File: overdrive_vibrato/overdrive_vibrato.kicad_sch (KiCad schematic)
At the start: 27 parts, among them J1 Conn_01x08, Q1 BC547, Q2 BC547, Q3 BC547, SW1 E-SWITCH-SW_Push_LED, SW2 E-SWITCH-SW_Push_LED, SW3 E-SWITCH-SW_Push_LED, U1 74HC14

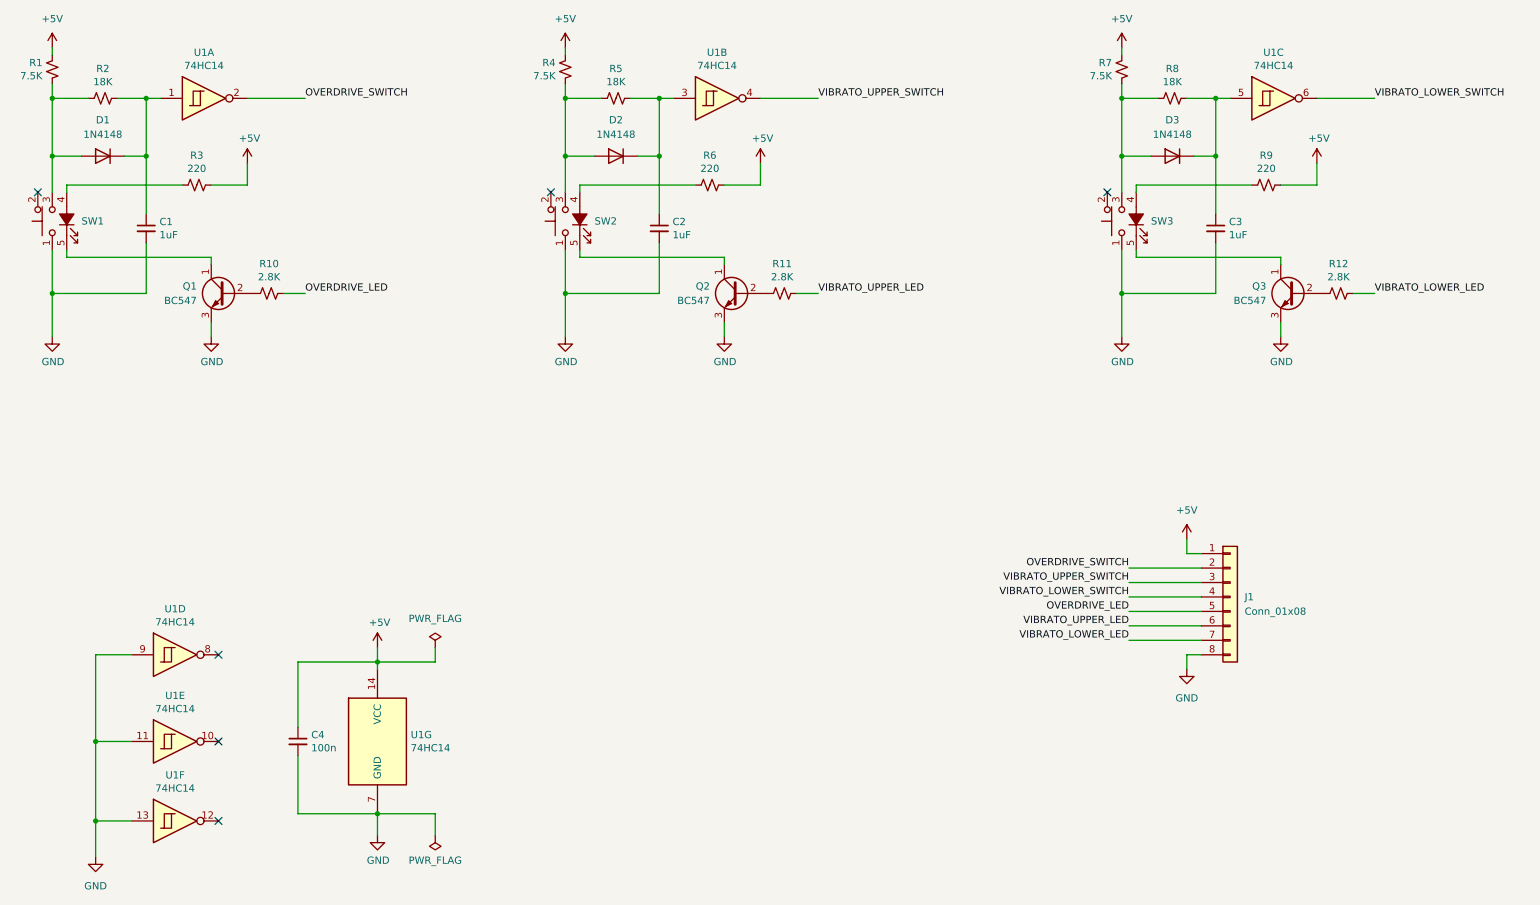
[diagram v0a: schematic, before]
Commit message: New organ architecture with mother board
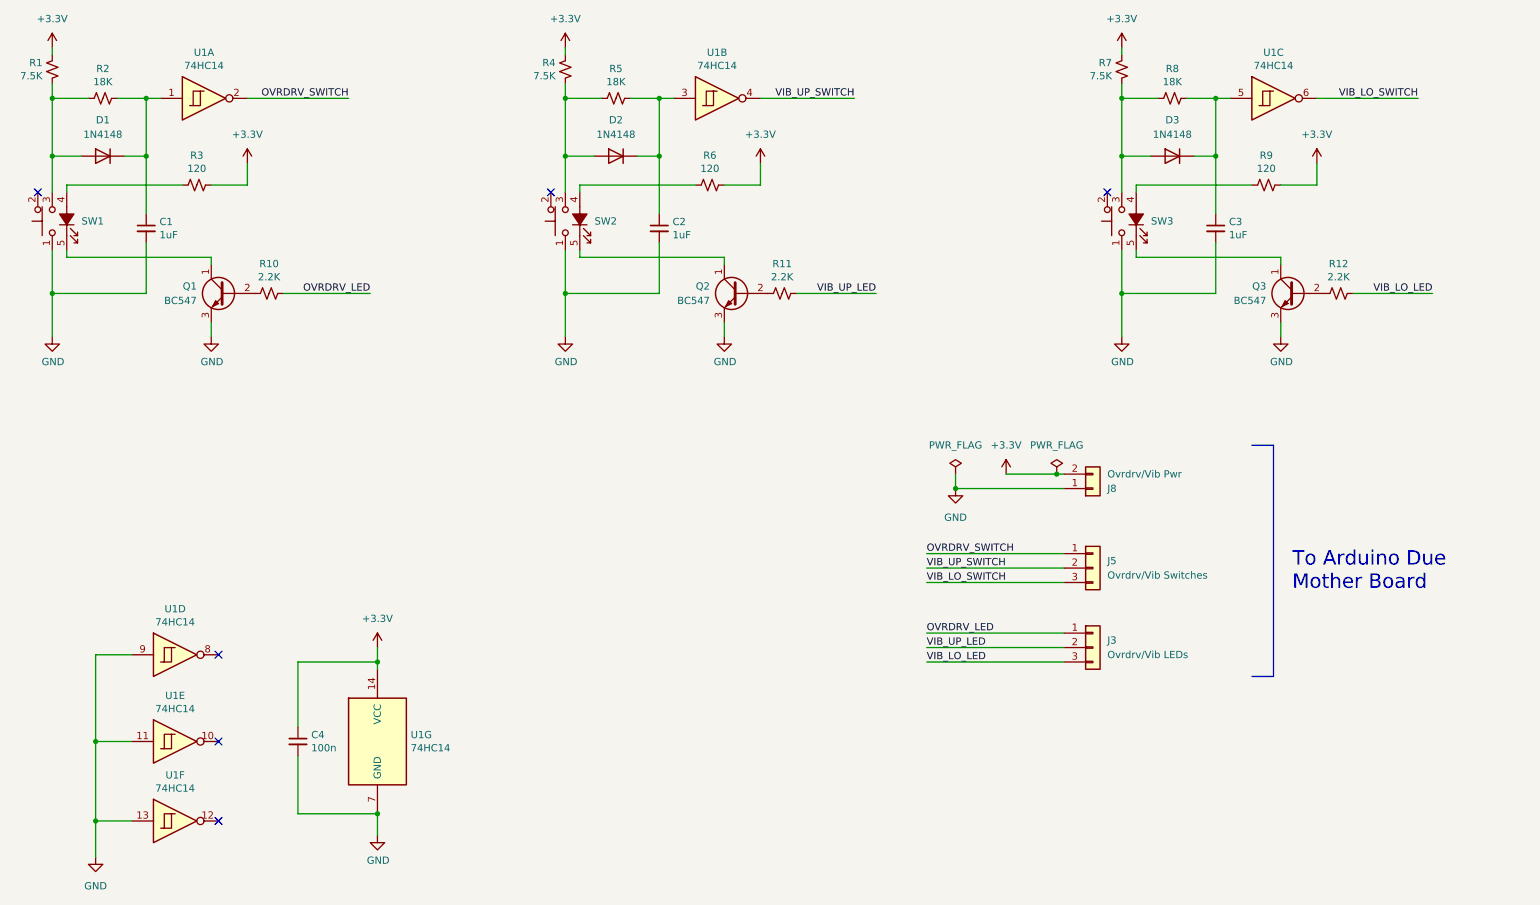
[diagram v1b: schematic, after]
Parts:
- removed J1: Conn_01x08, symbol Connector_Generic:Conn_01x08
- added J3: Ovrdrv/Vib LEDs, Connector_JST:JST_XH_B3B-XH-A_1x03_P2.50mm_Vertical, symbol Connector_Generic:Conn_01x03
- added J5: Ovrdrv/Vib Switches, Connector_JST:JST_XH_B3B-XH-A_1x03_P2.50mm_Vertical, symbol Connector_Generic:Conn_01x03
- added J8: Ovrdrv/Vib Pwr, Connector_JST:JST_XH_B2B-XH-A_1x02_P2.50mm_Vertical, symbol Connector_Generic:Conn_01x02
- R10, R11, R12: value 2.8K -> 2.2K
- R3, R6, R9: value 220 -> 120
- SW1, SW2, SW3: footprint b3_buttons_library:5511MBLKRED -> b3_footprints:5511MBLKRED
- U1: footprint Package_SO:SOIC-14_3.9x8.7mm_P1.27mm -> Package_DIP:DIP-14_W7.62mm_Socket_LongPads
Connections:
- net GND: now also J8.1 (Pin_1)
- net +5V renamed +3.3V
- net +3.3V: now also J8.2 (Pin_2)
- net OVERDRIVE_LED renamed OVRDRV_LED
- net OVRDRV_LED: now also J3.1 (Pin_1)
- net OVERDRIVE_SWITCH renamed OVRDRV_SWITCH
- net OVRDRV_SWITCH: now also J5.1 (Pin_1)
- net VIBRATO_LOWER_LED renamed VIB_LO_LED
- net VIB_LO_LED: now also J3.3 (Pin_3)
- net VIBRATO_LOWER_SWITCH renamed VIB_LO_SWITCH
- net VIB_LO_SWITCH: now also J5.3 (Pin_3)
- net VIBRATO_UPPER_LED renamed VIB_UP_LED
- net VIB_UP_LED: now also J3.2 (Pin_2)
- net VIBRATO_UPPER_SWITCH renamed VIB_UP_SWITCH
- net VIB_UP_SWITCH: now also J5.2 (Pin_2)
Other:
- note added: "To Arduino Due Mother Board"
